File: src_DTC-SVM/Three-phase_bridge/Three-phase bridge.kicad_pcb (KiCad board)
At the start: 2 copper layers, 419.1 x 318 mm, 94 parts, among them M1 MCP6022-I/P, M2 MCP6022-I/P, P1 CONN_1, P2 POWER_FUSE, P3 CONN_2, P4 CONN_1, P5 CONN_1, P6 POWER_FUSE, P7 CONN_1, P8 CONN_1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

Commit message: This is the PCB before editing the fill zones, the pads and clearance. The only inconsistency here is that the red Fill zones have chosen the wrong signals, so that the drain pins are not connected.
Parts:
- added STM32_CONN_Passive1: CONN_STM32_25X2_PASSIVE, PIN_ARRAY_STM32_25X2, F.Cu at (154.6, 171.2)
- moved 1PIN 52.8 mm to (202.4, 206.0)
- moved 1PIN 12.7 mm to (150.4, 132.1)
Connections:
- STM32_CONN1 pad 10: (no net) -> N-0000036
- STM32_CONN1 pad 11: (no net) -> N-0000052
- STM32_CONN1 pad 15: (no net) -> N-0000044
- STM32_CONN1 pad 16: (no net) -> N-0000038
- STM32_CONN1 pad 17: (no net) -> N-0000068
- STM32_CONN1 pad 18: (no net) -> N-0000033
- STM32_CONN1 pad 19: (no net) -> N-0000050
- STM32_CONN1 pad 20: (no net) -> N-0000039
- STM32_CONN1 pad 21: (no net) -> N-0000055
- STM32_CONN1 pad 22: (no net) -> N-0000040
- STM32_CONN1 pad 23: (no net) -> N-0000057
- STM32_CONN1 pad 24: (no net) -> N-0000041
- STM32_CONN1 pad 26: (no net) -> N-0000042
- STM32_CONN1 pad 31: (no net) -> N-0000056
- STM32_CONN1 pad 33: (no net) -> N-0000058
- STM32_CONN1 pad 35: (no net) -> N-0000064
- STM32_CONN1 pad 37: (no net) -> N-0000049
- STM32_CONN1 pad 39: (no net) -> N-0000028
- STM32_CONN1 pad 41: (no net) -> N-0000065
- STM32_CONN1 pad 43: (no net) -> N-0000047
- STM32_CONN1 pad 45: (no net) -> N-0000046
- STM32_CONN1 pad 46: (no net) -> N-0000031
- STM32_CONN1 pad 47: (no net) -> N-0000066
- STM32_CONN1 pad 48: (no net) -> N-0000032
- STM32_CONN1 pad 5: (no net) -> N-0000053
- STM32_CONN1 pad 6: (no net) -> N-0000034
- STM32_CONN1 pad 7: (no net) -> N-0000054
- STM32_CONN1 pad 8: (no net) -> N-0000035
- STM32_CONN1 pad 9: (no net) -> N-0000067
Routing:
- net GND: track 901.2 -> 929.4 mm
- net N-0000032: track 0.00 -> 15.1 mm
- net N-0000066: track 0.00 -> 15.1 mm
- net VDD: track 226.7 -> 240.8 mm
- net N-0000025: track 46.6 -> 43.0 mm
- net N-0000045: track 121.9 -> 124.9 mm
- added copper zone on F.Cu, net N-000008
- added copper zone on F.Cu, net N-0000082
- added copper zone on F.Cu, net N-0000083
- removed copper zone on F.Cu, net N-000006
- removed copper zone on F.Cu, net N-0000061
- removed copper zone on F.Cu, net N-0000062

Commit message: Connetions between the two stm32 connectors are finished.
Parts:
- moved 1PIN 53.1 mm to (149.4, 206.5)
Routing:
- net N-0000051: track 76.0 -> 104.8 mm
- net N-0000048: track 101.4 -> 129.8 mm
- net N-0000045: track 124.9 -> 151.9 mm
- net N-0000054: track 0.00 -> 16.1 mm
- net N-0000033: track 0.00 -> 15.5 mm
- net N-0000027: track 44.8 -> 60.1 mm
- net N-0000047: track 0.00 -> 15.3 mm
- net N-0000046: track 0.00 -> 15.3 mm
- net N-0000031: track 0.00 -> 15.3 mm
- net N-0000092: track 48.8 -> 64.1 mm
- net N-0000064: track 0.00 -> 15.2 mm
- net N-0000086: track 81.3 -> 96.5 mm
- net N-0000068: track 0.00 -> 15.2 mm
- net N-0000058: track 0.00 -> 15.2 mm
- net N-0000052: track 0.00 -> 15.2 mm
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- added copper zone on F.Cu, net N-0000062
- removed copper zone on F.Cu, net N-0000083
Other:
- net class Default: clearance 0.254 -> 0.0254
- rule trace_clearance: 0.254 -> 0.0254

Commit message: PCB files before globally editing the vías.
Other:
- net class Default: trace_width 0.254 -> 1.905; via_dia 0.889 -> 0.254; via_drill 0.635 -> 0.0762
- rule via_min_drill: 0.508 -> 0.0254
- rule via_min_size: 0.889 -> 0.0254

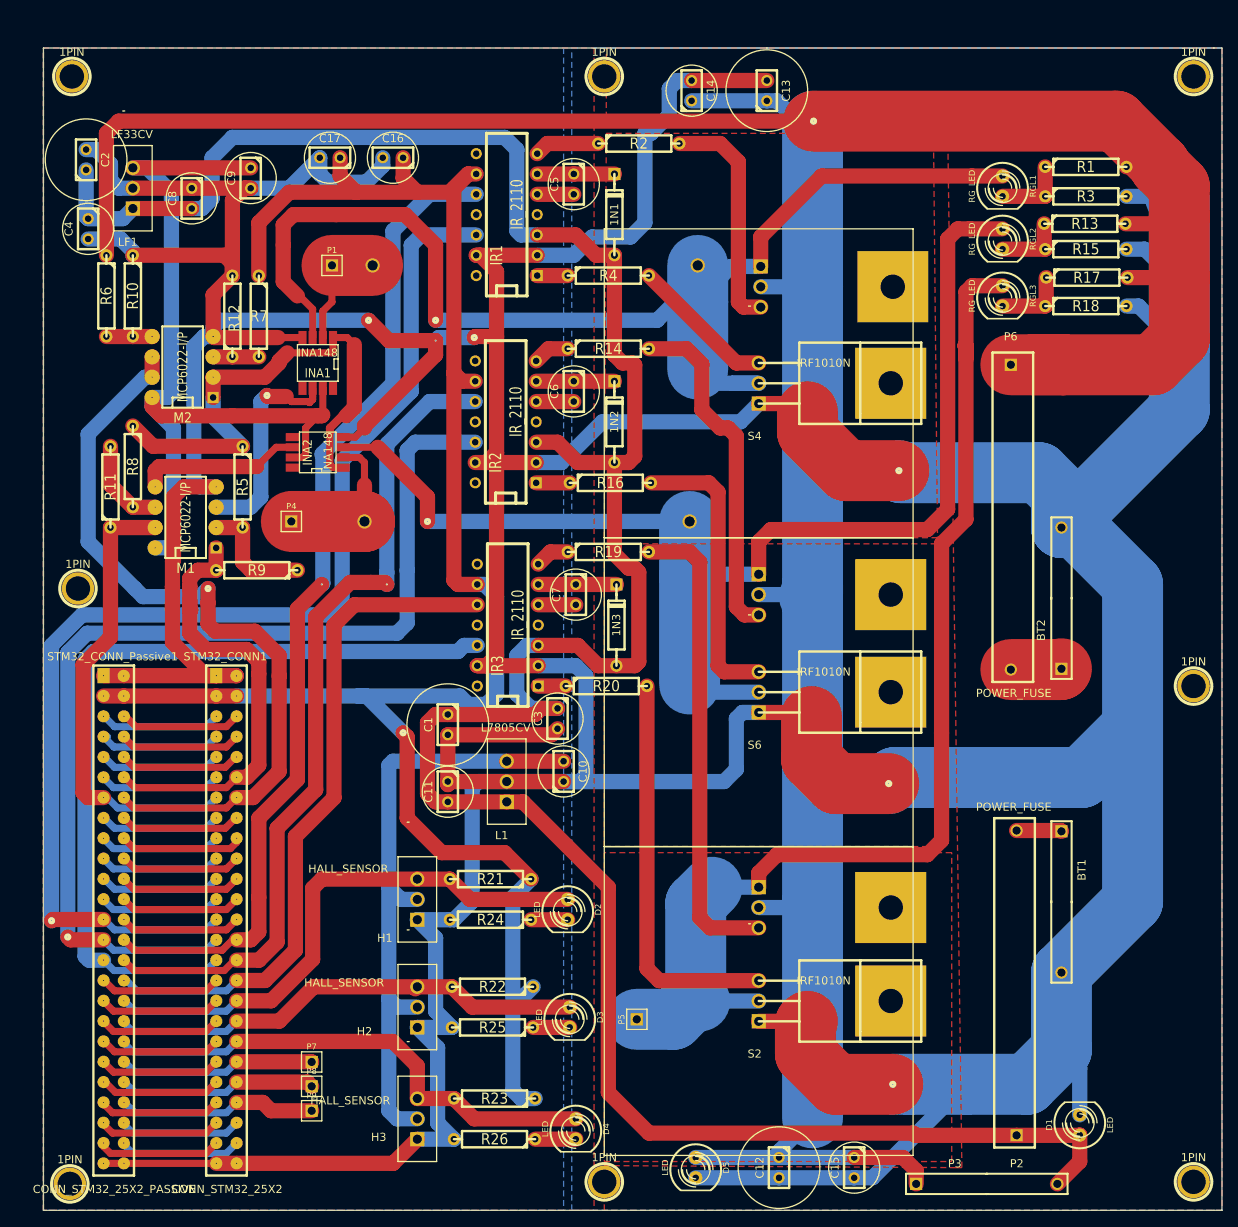
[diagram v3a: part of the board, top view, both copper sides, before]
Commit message: Before deleting fillzones.
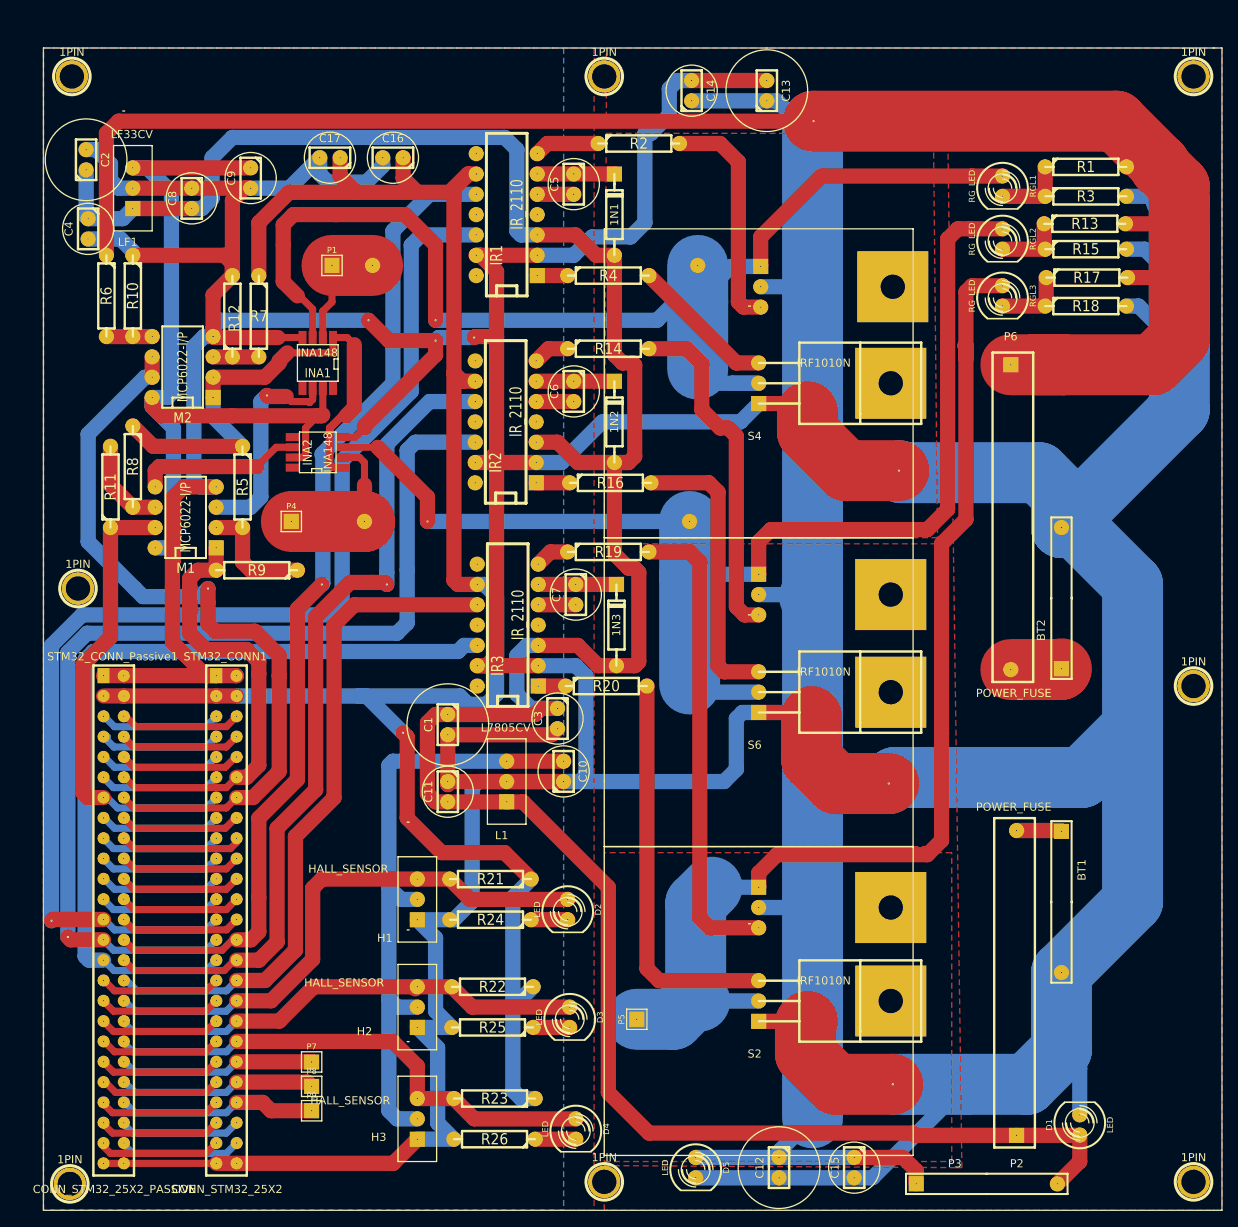
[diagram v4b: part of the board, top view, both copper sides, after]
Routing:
- removed copper zone on B.Cu, net +48V

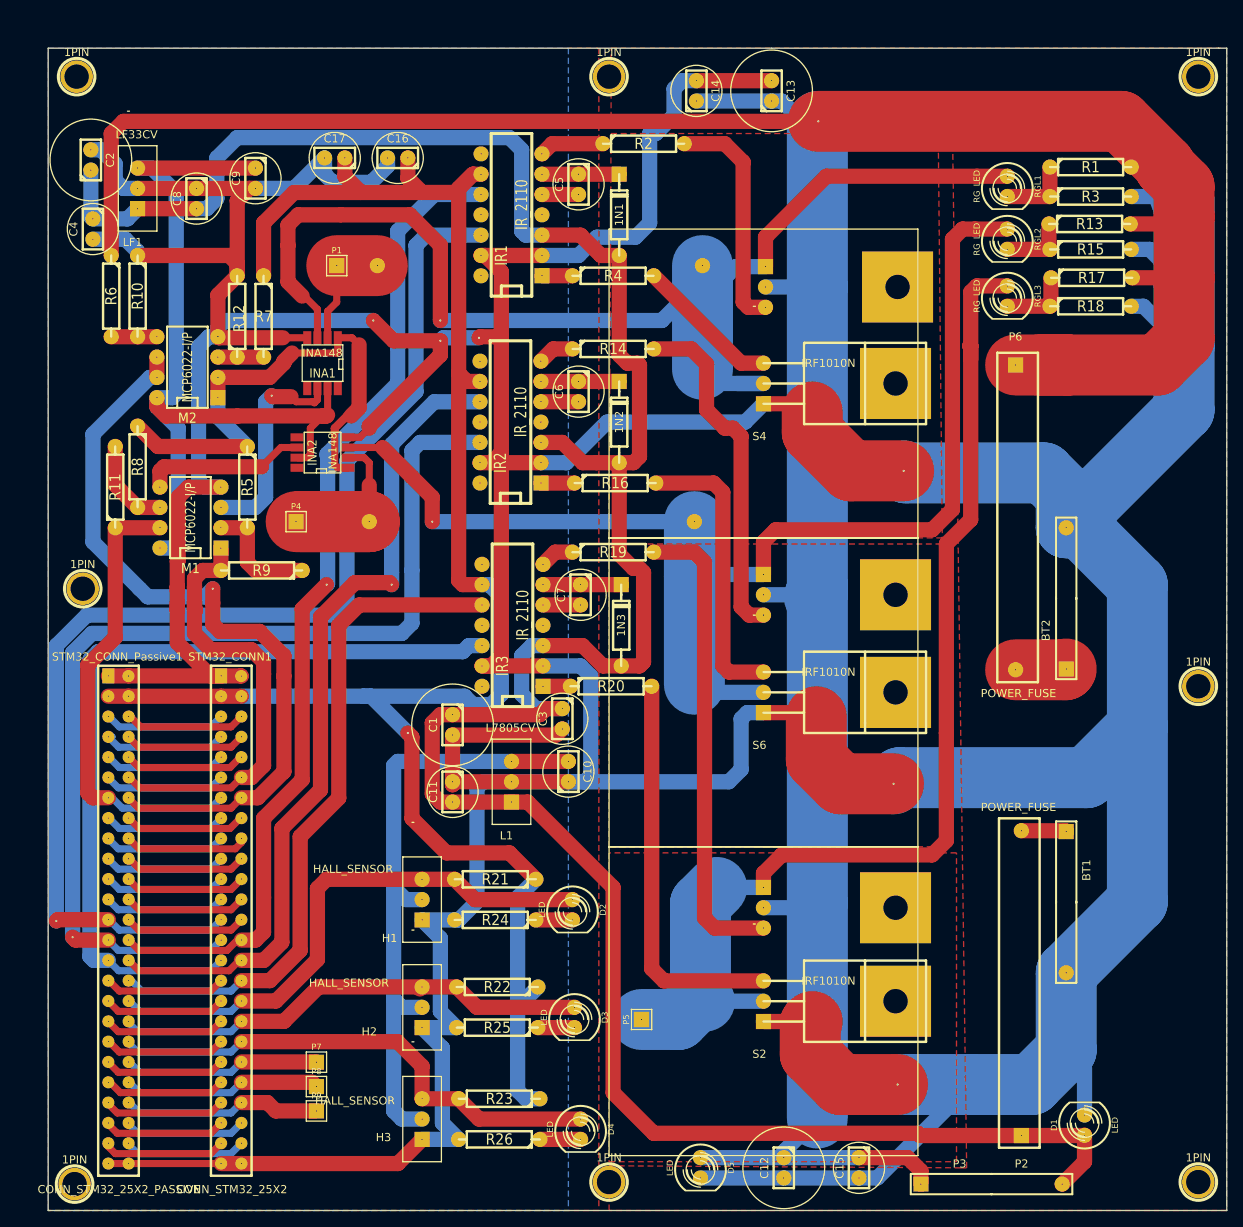
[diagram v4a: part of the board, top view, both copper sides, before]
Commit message: Fillzones completed. However, the schematic is damaged, looks incomplete and has interrogation signs in some modules.
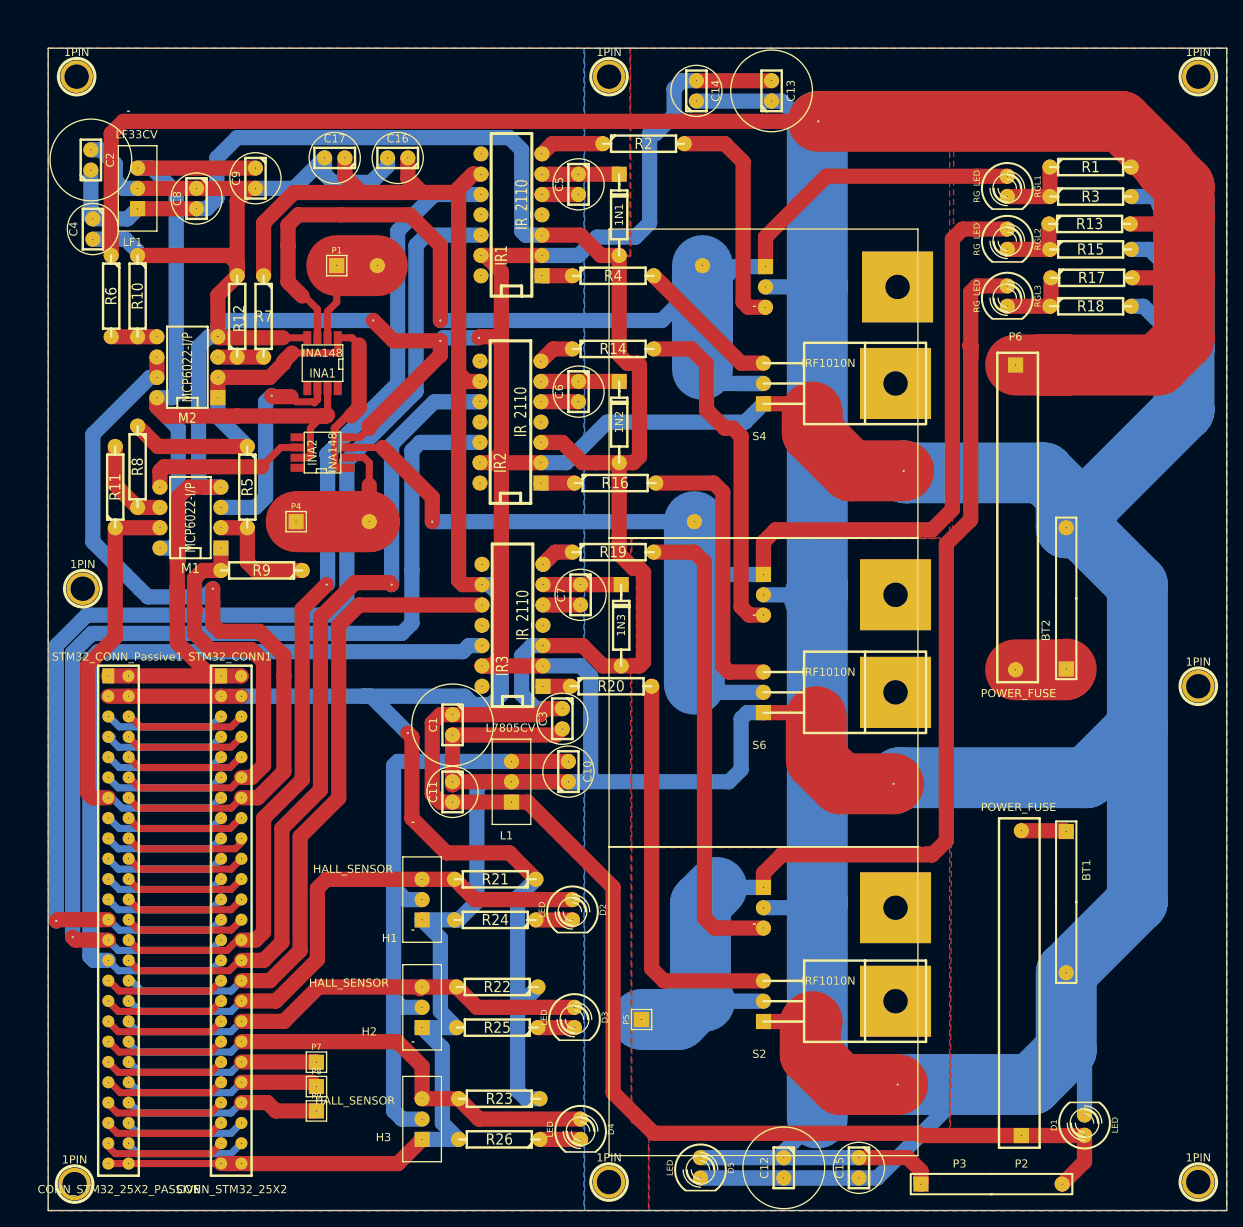
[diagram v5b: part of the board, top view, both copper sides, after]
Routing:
- added copper zone on B.Cu, net +48V
- added copper zone on F.Cu, net N-000006
- added copper zone on F.Cu, net N-0000061
- removed copper zone on F.Cu, net N-000008
- removed copper zone on F.Cu, net N-0000082
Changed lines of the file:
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@@
   (general
     (links 237)
-    (no_connects 6)
+    (no_connects 0)
     (area -125.780001 -108.254001 293.420001 210.058)
     (thickness 1.6)
@@
   (page A3)
   (layers
-    (15 F.Cu signal hide)
+    (15 F.Cu signal)
     (0 B.Cu signal)
     (16 B.Adhes user)
-    (17 F.Adhes user)
+    (17 F.Adhes user hide)
     (18 B.Paste user)
     (19 F.Paste user)
@@
   (segment (start 204.724 194.818) (end 204.724 184.404) (width 1.905) (layer B.Cu) (net 88))
   (segment (start 205.74 195.834) (end 204.724 194.818) (width 1.905) (layer B.Cu) (net 88))
-  (zone (net 63) (net_name N-0000062) (layer F.Cu) (hatch edge 0.508)
+  (zone (net 2) (net_name +48V) (layer B.Cu) (hatch edge 0.508)
     (connect_pads (clearance 0.0762))
     (min_thickness 0.0254)
-    (fill (arc_segments 16) (thermal_gap 0.0254) (thermal_bridge_width 1.524))
+    (fill (arc_segments 32) (thermal_gap 0.0762) (thermal_bridge_width 1.778))
     (polygon
       (pts
-        (xy 257.81 125.73) (xy 216.154 125.73) (xy 216.408 75.184) (xy 257.302 75.184)
+        (xy 293.37 209.804) (xy 213.106 209.804) (xy 213.106 64.516) (xy 293.37 64.516)
       )
     )
   )
-  (zone (net -1) (net_name N-0000082) (layer F.Cu) (hatch edge 0.508)
+  (zone (net 4) (net_name GND) (layer B.Cu) (hatch edge 0.508)
     (connect_pads (clearance 0.0762))
     (min_thickness 0.0254)
-    (fill (arc_segments 16) (thermal_gap 0.508) (thermal_bridge_width 0.508))
+    (fill (arc_segments 32) (thermal_gap 0.0762) (thermal_bridge_width 1.778))
     (polygon
       (pts
-        (xy 258.064 126.492) (xy 257.81 164.338) (xy 216.154 164.338) (xy 216.154 126.492)
+        (xy 213.0298 209.804) (xy 146.05 209.804) (xy 146.05 64.516) (xy 213.0298 64.516)
       )
     )
   )
-  (zone (net 77) (net_name N-000008) (layer F.Cu) (hatch edge 0.508)
+  (zone (net 60) (net_name N-000006) (layer F.Cu) (hatch edge 0.508)
     (connect_pads (clearance 0.0762))
     (min_thickness 0.0254)
-    (fill (arc_segments 16) (thermal_gap 0.508) (thermal_bridge_width 0.508))
+    (fill (arc_segments 32) (thermal_gap 0.0762) (thermal_bridge_width 1.778))
     (polygon
       (pts
-        (xy 216.154 165.1) (xy 216.154 203.708) (xy 259.588 203.708) (xy 259.588 165.1)
+        (xy 258.7244 200.3044) (xy 222.0214 200.3044) (xy 218.9988 198.6788) (xy 218.9988 164.4396) (xy 258.7244 164.4396)
       )
     )
   )
-  (zone (net 4) (net_name GND) (layer B.Cu) (hatch edge 0.508)
+  (zone (net 62) (net_name N-0000061) (layer F.Cu) (hatch edge 0.508)
+    (connect_pads (clearance 0.0762))
+    (min_thickness 0.0254)
+    (fill (arc_segments 32) (thermal_gap 0.0762) (thermal_bridge_width 1.778))
+    (polygon
+      (pts
+        (xy 258.7498 125.8062) (xy 258.7244 164.338) (xy 218.9988 164.338) (xy 218.9988 141.4526) (xy 220.4466 141.4526)
+        (xy 220.4212 129.8956) (xy 218.9988 129.8956) (xy 218.9988 125.8316)
+      )
+    )
+  )
+  (zone (net 63) (net_name N-0000062) (layer F.Cu) (hatch edge 0.508)
     (connect_pads (clearance 0.0762))
     (min_thickness 0.0254)
-    (fill (arc_segments 16) (thermal_gap 0.508) (thermal_bridge_width 0.508))
+    (fill (arc_segments 32) (thermal_gap 0.0762) (thermal_bridge_width 1.778))
     (polygon
       (pts
-        (xy 211.074 209.804) (xy 146.05 209.804) (xy 146.05 64.516) (xy 211.074 64.516)
+        (xy 218.8718 125.8316) (xy 218.8718 128.016) (xy 217.297 126.873) (xy 217.2716 123.0122) (xy 217.3224 116.1796)
+        (xy 219.8878 115.3668) (xy 219.5576 103.8352) (xy 217.2716 103.2002) (xy 217.17 90.551) (xy 218.8718 90.5256)
+        (xy 218.8718 73.914) (xy 258.7244 73.914) (xy 258.7244 125.73) (xy 218.8718 125.73) (xy 218.8718 125.8316)
       )
     )
@@
     (connect_pads (clearance 0.0762))
     (min_thickness 0.0254)
-    (fill (arc_segments 16) (thermal_gap 0.508) (thermal_bridge_width 0.508))
+    (fill (arc_segments 32) (thermal_gap 0.0762) (thermal_bridge_width 1.778))
     (polygon
       (pts
-        (xy 293.37 209.804) (xy 216.154 209.804) (xy 216.154 204.216) (xy 260.096 204.47) (xy 260.858 204.47)
-        (xy 259.08 74.422) (xy 216.408 74.422) (xy 216.408 64.516) (xy 293.37 64.516)
+        (xy 293.3954 64.4906) (xy 293.37 209.8294) (xy 221.1578 209.8294) (xy 221.1578 200.5838) (xy 258.826 200.5076)
+        (xy 259.2578 73.2282) (xy 218.8464 73.2282) (xy 218.8464 64.4906)
       )
     )
@@
     (connect_pads (clearance 0.0762))
     (min_thickness 0.0254)
-    (fill (arc_segments 16) (thermal_gap 0.508) (thermal_bridge_width 0.508))
+    (fill (arc_segments 32) (thermal_gap 0.0762) (thermal_bridge_width 1.778))
     (polygon
       (pts
-        (xy 214.884 209.804) (xy 146.05 209.804) (xy 146.05 64.516) (xy 214.884 64.516)
+        (xy 221.0816 209.8294) (xy 146.0246 209.8294) (xy 146.0246 64.4906) (xy 218.7702 64.4906) (xy 218.7702 72.6948)
+        (xy 218.7448 72.8218) (xy 218.7956 90.424) (xy 218.2876 90.424) (xy 217.0938 90.3732) (xy 216.789 103.0478)
+        (xy 219.202 104.5464) (xy 219.2274 115.4684) (xy 216.5604 115.4684) (xy 216.535 127.4826) (xy 216.5858 127.9398)
+        (xy 216.8652 128.3716) (xy 217.7542 129.2606) (xy 219.5576 130.4036) (xy 219.5576 140.8176) (xy 218.8464 140.8176)
+        (xy 218.8464 142.494) (xy 218.9226 195.9864) (xy 218.9226 198.7296) (xy 219.1258 198.8566) (xy 219.2528 198.9074)
+        (xy 219.5068 199.1868) (xy 221.0816 200.3044)
       )
     )
